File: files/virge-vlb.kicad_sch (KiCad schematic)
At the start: 38 parts, among them J2 VGA, J3 VESA feature, U1 86C375, Y1 14.318MHz

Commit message: PCB work
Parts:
- added R34: 10K, Resistor_SMD:R_0805_2012Metric_Pad1.20x1.40mm_HandSolder, symbol Device:R
- FB1, FB2, FB3: footprint (none) -> Inductor_THT:L_Axial_L9.5mm_D4.0mm_P15.24mm_Horizontal_Fastron_SMCC
- J3: footprint (none) -> Connector_PinHeader_2.54mm:PinHeader_2x13_P2.54mm_Vertical
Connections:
- net VCC: now also R34.2
- net at U1.165 (~{PDOWN}): now also R34.1
- net ESYNC: now reaches U1.205 (SPCLK/ESYNC)
- net ESYNC: now also R28.2
- no-connect marks 2 -> 6
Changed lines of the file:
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@@
   (junction (at 208.28 49.53) (diameter 0) (color 0 0 0 0)
   )
+  (no_connect (at 86.36 163.83))
   (no_connect (at 44.45 69.85))
+  (no_connect (at 86.36 148.59))
+  (no_connect (at 173.99 59.69))
+  (no_connect (at 86.36 161.29))
   (no_connect (at 29.21 85.09))
   (wire (pts (xy 173.99 27.94) (xy 173.99 36.83))
@@
     (stroke (width 0) (type default))
   )
+  (wire (pts (xy 163.83 64.77) (xy 173.99 64.77))
+    (stroke (width 0) (type default))
+  )
   (wire (pts (xy 163.83 72.39) (xy 173.99 72.39))
     (stroke (width 0) (type default))
@@
     (stroke (width 0) (type default))
   )
+  (wire (pts (xy 154.94 52.07) (xy 154.94 57.15))
+    (stroke (width 0) (type default))
+  )
   (wire (pts (xy 82.55 135.89) (xy 82.55 151.13))
     (stroke (width 0) (type default))
@@
   )
   (wire (pts (xy 29.21 107.95) (xy 29.21 109.22))
+    (stroke (width 0) (type default))
+  )
+  (wire (pts (xy 162.56 57.15) (xy 173.99 57.15))
     (stroke (width 0) (type default))
   )
@@
     (effects (font (size 1.27 1.27)) (justify right bottom))
   )
+  (label "ESYNC" (at 163.83 64.77 0) (fields_autoplaced)
+    (effects (font (size 1.27 1.27)) (justify left bottom))
+  )
   (label "S3_GREEN" (at 130.81 80.01 180) (fields_autoplaced)
     (effects (font (size 1.27 1.27)) (justify right bottom))
@@
   )
   (label "S3_RED" (at 163.83 41.91 0) (fields_autoplaced)
+    (effects (font (size 1.27 1.27)) (justify left bottom))
+  )
+  (label "ESYNC" (at 40.64 146.05 0) (fields_autoplaced)
     (effects (font (size 1.27 1.27)) (justify left bottom))
   )
@@
       (effects (font (size 1.27 1.27)))
     )
-    (property "Footprint" "" (at 91.44 148.59 0)
+    (property "Footprint" "Connector_PinHeader_2.54mm:PinHeader_2x13_P2.54mm_Vertical" (at 91.44 148.59 0)
       (effects (font (size 1.27 1.27)) hide)
     )
@@
     )
   )
+  (symbol (lib_id "power:VCC") (at 154.94 52.07 0) (unit 1)
+    (in_bom yes) (on_board yes) (dnp no) (fields_autoplaced)
+    (property "Reference" "#PWR031" (at 154.94 55.88 0)
+      (effects (font (size 1.27 1.27)) hide)
+    )
+    (property "Value" "VCC" (at 154.94 48.26 0)
+      (effects (font (size 1.27 1.27)))
+    )
+    (property "Footprint" "" (at 154.94 52.07 0)
+      (effects (font (size 1.27 1.27)) hide)
+    )
+    (property "Datasheet" "" (at 154.94 52.07 0)
+      (effects (font (size 1.27 1.27)) hide)
+    )
+    (pin "1")
+    (instances
+      (project "virge-vlb"
+        (path "/e8216711-86b5-4276-82f4-4c7ed22b9a9c"
+          (reference "#PWR031") (unit 1)
+        )
+      )
+    )
+  )
   (symbol (lib_id "Connector_Generic:Conn_01x02") (at 58.42 67.31 0) (unit 1)
     (in_bom yes) (on_board yes) (dnp no)
@@
       (effects (font (size 1.27 1.27)) hide)
     )
-    (property "Footprint" "" (at 85.09 86.868 90)
+    (property "Footprint" "Inductor_THT:L_Axial_L9.5mm_D4.0mm_P15.24mm_Horizontal_Fastron_SMCC" (at 85.09 86.868 90)
       (effects (font (size 1.27 1.27)) hide)
     )
@@
       (effects (font (size 1.27 1.27)) hide)
     )
-    (property "Footprint" "" (at 86.36 76.708 90)
+    (property "Footprint" "Inductor_THT:L_Axial_L9.5mm_D4.0mm_P15.24mm_Horizontal_Fastron_SMCC" (at 86.36 76.708 90)
       (effects (font (size 1.27 1.27)) hide)
     )
@@
     )
   )
-  (symbol (lib_id "Device:C") (at 67.31 91.44 0) (unit 1)
-    (in_bom yes) (on_board yes) (dnp no)
-    (property "Reference" "C5" (at 69.85 90.17 0)
-      (effects (font (size 1.27 1.27)) (justify left))
-    )
-    (property "Value" "10pF" (at 69.85 93.98 0)
-      (effects (font (size 1.27 1.27)) (justify left))
-    )
-    (property "Footprint" "Capacitor_SMD:C_0805_2012Metric_Pad1.18x1.45mm_HandSolder" (at 68.2752 95.25 0)
-      (effects (font (size 1.27 1.27)) hide)
-    )
-    (property "Datasheet" "~" (at 67.31 91.44 0)
-      (effects (font (size 1.27 1.27)) hide)
-    )
-    (pin "1")
-    (pin "2")
-    (instances
-      (project "virge-vlb"
-        (path "/e8216711-86b5-4276-82f4-4c7ed22b9a9c"
-          (reference "C5") (unit 1)
-        )
-      )
-    )
-  )
-  (symbol (lib_id "power:VCC") (at 215.9 31.75 0) (unit 1)
-    (in_bom yes) (on_board yes) (dnp no) (fields_autoplaced)
-    (property "Reference" "#PWR01" (at 215.9 35.56 0)
-      (effects (font (size 1.27 1.27)) hide)
-    )
-    (property "Value" "VCC" (at 215.9 27.94 0)
-      (effects (font (size 1.27 1.27)))
-    )
-    (property "Footprint" "" (at 215.9 31.75 0)
-      (effects (font (size 1.27 1.27)) hide)
-    )
-    (property "Datasheet" "" (at 215.9 31.75 0)
-      (effects (font (size 1.27 1.27)) hide)
-    )
-    (pin "1")
-    (instances
-      (project "virge-vlb"
-        (path "/e8216711-86b5-4276-82f4-4c7ed22b9a9c"
-          (reference "#PWR01") (unit 1)
-        )
-      )
-    )
-  )
-  (symbol (lib_id "Device:R") (at 78.74 134.62 0) (unit 1)
-    (in_bom yes) (on_board yes) (dnp no)
-    (property "Reference" "R27" (at 80.01 130.81 0)
-      (effects (font (size 1.27 1.27)) (justify left))
-    )
-    (property "Value" "4K7" (at 80.01 133.35 0)
-      (effects (font (size 1.27 1.27)) (justify left))
-    )
-    (property "Footprint" "Resistor_SMD:R_0805_2012Metric_Pad1.20x1.40mm_HandSolder" (at 76.962 134.62 90)
-      (effects (font (size 1.27 1.27)) hide)
-    )
-    (property "Datasheet" "~" (at 78.74 134.62 0)
-      (effects (font (size 1.27 1.27)) hide)
-    )
-    (pin "1")
-    (pin "2")
-    (instances
-      (project "virge-vlb"
-        (path "/e8216711-86b5-4276-82f4-4c7ed22b9a9c"
-          (reference "R27") (unit 1)
+  (symbol (lib_id "Device:R") (at 158.75 57.15 270) (unit 1)
+    (in_bom yes) (on_board yes) (dnp no)
+    (property "Reference" "R34" (at 157.48 54.61 90)
+      (effects (font (size 1.27 1.27)) (justify left))
+    )
+    (property "Value" "10K" (at 157.48 59.69 90)
+      (effects (font (size 1.27 1.27)) (justify left))
+    )
+    (property "Footprint" "Resistor_SMD:R_0805_2012Metric_Pad1.20x1.40mm_HandSolder" (at 158.75 55.372 90)
+      (effects (font (size 1.27 1.27)) hide)
+    )
+    (property "Datasheet" "~" (at 158.75 57.15 0)
+      (effects (font (size 1.27 1.27)) hide)
+    )
+    (pin "1")
+    (pin "2")
+    (instances
+      (project "virge-vlb"
+        (path "/e8216711-86b5-4276-82f4-4c7ed22b9a9c"
+          (reference "R34") (unit 1)
         )
         (path "/e8216711-86b5-4276-82f4-4c7ed22b9a9c/73bb2a59-bfac-4efc-8051-53849b0f9066"
@@
     )
   )
+  (symbol (lib_id "Device:C") (at 67.31 91.44 0) (unit 1)
+    (in_bom yes) (on_board yes) (dnp no)
+    (property "Reference" "C5" (at 69.85 90.17 0)
+      (effects (font (size 1.27 1.27)) (justify left))
+    )
+    (property "Value" "10pF" (at 69.85 93.98 0)
+      (effects (font (size 1.27 1.27)) (justify left))
+    )
+    (property "Footprint" "Capacitor_SMD:C_0805_2012Metric_Pad1.18x1.45mm_HandSolder" (at 68.2752 95.25 0)
+      (effects (font (size 1.27 1.27)) hide)
+    )
+    (property "Datasheet" "~" (at 67.31 91.44 0)
+      (effects (font (size 1.27 1.27)) hide)
+    )
+    (pin "1")
+    (pin "2")
+    (instances
+      (project "virge-vlb"
+        (path "/e8216711-86b5-4276-82f4-4c7ed22b9a9c"
+          (reference "C5") (unit 1)
+        )
+      )
+    )
+  )
+  (symbol (lib_id "power:VCC") (at 215.9 31.75 0) (unit 1)
+    (in_bom yes) (on_board yes) (dnp no) (fields_autoplaced)
+    (property "Reference" "#PWR01" (at 215.9 35.56 0)
+      (effects (font (size 1.27 1.27)) hide)
+    )
+    (property "Value" "VCC" (at 215.9 27.94 0)
+      (effects (font (size 1.27 1.27)))
+    )
+    (property "Footprint" "" (at 215.9 31.75 0)
+      (effects (font (size 1.27 1.27)) hide)
+    )
+    (property "Datasheet" "" (at 215.9 31.75 0)
+      (effects (font (size 1.27 1.27)) hide)
+    )
+    (pin "1")
+    (instances
+      (project "virge-vlb"
+        (path "/e8216711-86b5-4276-82f4-4c7ed22b9a9c"
+          (reference "#PWR01") (unit 1)
+        )
+      )
+    )
+  )
+  (symbol (lib_id "Device:R") (at 78.74 134.62 0) (unit 1)
+    (in_bom yes) (on_board yes) (dnp no)
+    (property "Reference" "R27" (at 80.01 130.81 0)
+      (effects (font (size 1.27 1.27)) (justify left))
+    )
+    (property "Value" "4K7" (at 80.01 133.35 0)
+      (effects (font (size 1.27 1.27)) (justify left))
+    )
+    (property "Footprint" "Resistor_SMD:R_0805_2012Metric_Pad1.20x1.40mm_HandSolder" (at 76.962 134.62 90)
+      (effects (font (size 1.27 1.27)) hide)
+    )
+    (property "Datasheet" "~" (at 78.74 134.62 0)
+      (effects (font (size 1.27 1.27)) hide)
+    )
+    (pin "1")
+    (pin "2")
+    (instances
+      (project "virge-vlb"
+        (path "/e8216711-86b5-4276-82f4-4c7ed22b9a9c"
+          (reference "R27") (unit 1)
+        )
+        (path "/e8216711-86b5-4276-82f4-4c7ed22b9a9c/73bb2a59-bfac-4efc-8051-53849b0f9066"
+          (reference "R16") (unit 1)
+        )
+      )
+    )
+  )
   (symbol (lib_id "Device:FerriteBead") (at 92.71 80.01 90) (unit 1)
     (in_bom yes) (on_board yes) (dnp no) (fields_autoplaced)
@@
       (effects (font (size 1.27 1.27)) hide)
     )
-    (property "Footprint" "" (at 92.71 81.788 90)
-      (effects (font (size 1.27 1.27)) hide)
-    )
+    (property "Footprint" "Inductor_THT:L_Axial_L9.5mm_D4.0mm_P15.24mm_Horizontal_Fastron_SMCC" (at 92.71 81.788 90)
+      (effects (font (size 1.27 1.27)) hide)
+    )

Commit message: even more PCB work
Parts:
- FB1: renamed from FB3; footprint Inductor_THT:L_Axial_L9.5mm_D4.0mm_P15.24mm_Horizontal_Fastron_SMCC -> Inductor_SMD:L_0805_2012Metric_Pad1.15x1.40mm_HandSolder
- FB2: footprint Inductor_THT:L_Axial_L9.5mm_D4.0mm_P15.24mm_Horizontal_Fastron_SMCC -> Inductor_SMD:L_0805_2012Metric_Pad1.15x1.40mm_HandSolder
- FB3: renamed from FB1; footprint Inductor_THT:L_Axial_L9.5mm_D4.0mm_P15.24mm_Horizontal_Fastron_SMCC -> Inductor_SMD:L_0805_2012Metric_Pad1.15x1.40mm_HandSolder
- U1: value 86C375 -> 86C325
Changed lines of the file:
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@@
       (effects (font (size 1.524 1.524)) (justify left))
     )
-    (property "Value" "86C375" (at 138.43 144.145 0)
+    (property "Value" "86C325" (at 138.43 144.145 0)
       (effects (font (size 1.524 1.524)) (justify left))
     )
@@
   (symbol (lib_id "Device:FerriteBead") (at 85.09 85.09 90) (unit 1)
     (in_bom yes) (on_board yes) (dnp no) (fields_autoplaced)
-    (property "Reference" "FB3" (at 85.0392 81.28 90)
+    (property "Reference" "FB1" (at 85.0392 81.28 90)
       (effects (font (size 1.27 1.27)))
     )
@@
       (effects (font (size 1.27 1.27)) hide)
     )
-    (property "Footprint" "Inductor_THT:L_Axial_L9.5mm_D4.0mm_P15.24mm_Horizontal_Fastron_SMCC" (at 85.09 86.868 90)
+    (property "Footprint" "Inductor_SMD:L_0805_2012Metric_Pad1.15x1.40mm_HandSolder" (at 85.09 86.868 90)
       (effects (font (size 1.27 1.27)) hide)
     )
@@
       (project "virge-vlb"
         (path "/e8216711-86b5-4276-82f4-4c7ed22b9a9c"
-          (reference "FB3") (unit 1)
+          (reference "FB1") (unit 1)
         )
       )
@@
       (effects (font (size 1.524 1.524)))
     )
-    (property "Value" "86C375" (at 191.135 33.02 0)
+    (property "Value" "86C325" (at 191.135 33.02 0)
       (effects (font (size 1.524 1.524)))
     )
@@
   (symbol (lib_id "Device:FerriteBead") (at 86.36 74.93 90) (unit 1)
     (in_bom yes) (on_board yes) (dnp no) (fields_autoplaced)
-    (property "Reference" "FB1" (at 86.3092 71.12 90)
+    (property "Reference" "FB3" (at 86.3092 71.12 90)
       (effects (font (size 1.27 1.27)))
     )
@@
       (effects (font (size 1.27 1.27)) hide)
     )
-    (property "Footprint" "Inductor_THT:L_Axial_L9.5mm_D4.0mm_P15.24mm_Horizontal_Fastron_SMCC" (at 86.36 76.708 90)
+    (property "Footprint" "Inductor_SMD:L_0805_2012Metric_Pad1.15x1.40mm_HandSolder" (at 86.36 76.708 90)
       (effects (font (size 1.27 1.27)) hide)
     )
@@
       (project "virge-vlb"
         (path "/e8216711-86b5-4276-82f4-4c7ed22b9a9c"
-          (reference "FB1") (unit 1)
+          (reference "FB3") (unit 1)
         )
       )
@@
       (effects (font (size 1.27 1.27)) hide)
     )
-    (property "Footprint" "Inductor_THT:L_Axial_L9.5mm_D4.0mm_P15.24mm_Horizontal_Fastron_SMCC" (at 92.71 81.788 90)
-      (effects (font (size 1.27 1.27)) hide)
-    )
+    (property "Footprint" "Inductor_SMD:L_0805_2012Metric_Pad1.15x1.40mm_HandSolder" (at 92.71 81.788 90)
+      (effects (font (size 1.27 1.27)) hide)
+    )

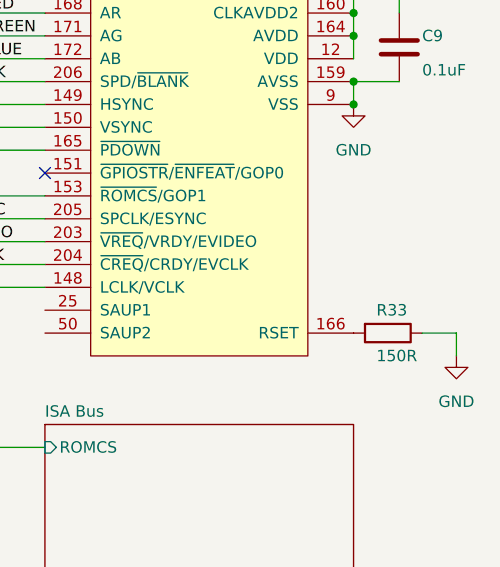
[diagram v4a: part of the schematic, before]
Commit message: added VREF R for fine tuning
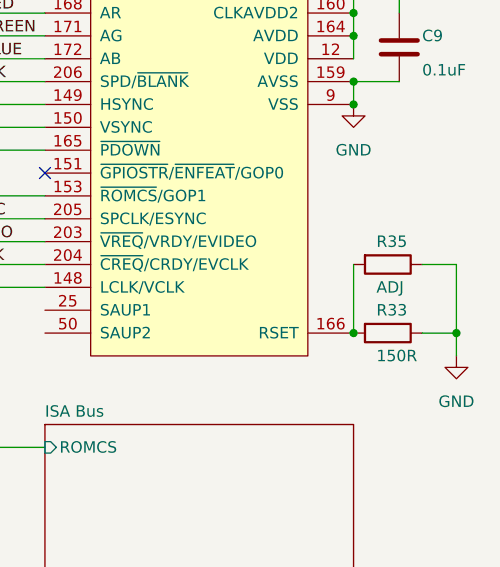
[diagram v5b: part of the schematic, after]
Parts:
- added R35: ADJ, Resistor_SMD:R_0805_2012Metric_Pad1.20x1.40mm_HandSolder, symbol Device:R
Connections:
- net GND: now also R35.1
- net at R33.2, U1.166 (RSET): now also R35.2
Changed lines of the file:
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@@
 (kicad_sch (version 20230121) (generator eeschema)
   (paper "A4")
+  (junction (at 219.71 77.47) (diameter 0) (color 0 0 0 0)
+  )
   (junction (at 58.42 146.05) (diameter 0) (color 0 0 0 0)
   )
@@
   )
   (junction (at 95.25 99.06) (diameter 0) (color 0 0 0 0)
+  )
+  (junction (at 208.28 77.47) (diameter 0) (color 0 0 0 0)
   )
   (junction (at 67.31 80.01) (diameter 0) (color 0 0 0 0)
@@
     (stroke (width 0) (type default))
   )
+  (wire (pts (xy 215.9 69.85) (xy 219.71 69.85))
+    (stroke (width 0) (type default))
+  )
   (wire (pts (xy 166.37 27.94) (xy 166.37 39.37))
     (stroke (width 0) (type default))
@@
     (stroke (width 0) (type default))
   )
+  (wire (pts (xy 219.71 69.85) (xy 219.71 77.47))
+    (stroke (width 0) (type default))
+  )
   (wire (pts (xy 119.38 74.93) (xy 119.38 91.44))
     (stroke (width 0) (type default))
@@
   )
   (wire (pts (xy 29.21 107.95) (xy 29.21 109.22))
+    (stroke (width 0) (type default))
+  )
+  (wire (pts (xy 208.28 69.85) (xy 208.28 77.47))
     (stroke (width 0) (type default))
   )
@@
         )
         (path "/e8216711-86b5-4276-82f4-4c7ed22b9a9c/73bb2a59-bfac-4efc-8051-53849b0f9066"
+          (reference "R16") (unit 1)
+        )
+      )
+    )
+  )
+  (symbol (lib_id "Device:R") (at 212.09 69.85 270) (unit 1)
+    (in_bom yes) (on_board yes) (dnp no)
+    (property "Reference" "R35" (at 210.82 67.31 90)
+      (effects (font (size 1.27 1.27)) (justify left))
+    )
+    (property "Value" "ADJ" (at 210.82 72.39 90)
+      (effects (font (size 1.27 1.27)) (justify left))
+    )
+    (property "Footprint" "Resistor_SMD:R_0805_2012Metric_Pad1.20x1.40mm_HandSolder" (at 212.09 68.072 90)
+      (effects (font (size 1.27 1.27)) hide)
+    )
+    (property "Datasheet" "~" (at 212.09 69.85 0)
+      (effects (font (size 1.27 1.27)) hide)
+    )
+    (pin "1")
+    (pin "2")
+    (instances
+      (project "virge-vlb"
+        (path "/e8216711-86b5-4276-82f4-4c7ed22b9a9c"
+          (reference "R35") (unit 1)
+        )
+        (path "/e8216711-86b5-4276-82f4-4c7ed22b9a9c/73bb2a59-bfac-4efc-8051-53849b0f9066"

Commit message: initial PCB routed
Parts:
- added C10, C11, C12, C13, C14: 0.1uF, Capacitor_SMD:C_0805_2012Metric_Pad1.18x1.45mm_HandSolder, symbol Device:C
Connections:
- net GND: now also C10.2, C11.2, C12.2, C13.2, C14.2
- net VCC: now also C10.1, C11.1, C12.1, C13.1, C14.1
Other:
- sheet ISA Bus ports: added none; removed IRQ2
- sheet VL Bus ports: added none; removed IRQ2
